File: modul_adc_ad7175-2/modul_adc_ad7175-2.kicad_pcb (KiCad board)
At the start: 2 copper layers, 61 x 55.9 mm, 9 parts

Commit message: Приступил к разводке платы c AD7175-2.
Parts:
- added C1: 4.7 мк, IWsmd_case:SMD0805, F.Cu at (76.5, 138.4)
- added C10: 270 п, IWsmd_case:SMD0805, F.Cu at (98.6, 114.3)
- added C11: 270 п, IWsmd_case:SMD0805, F.Cu at (95.5, 126.2)
- added C12: 270 п, IWsmd_case:SMD0805, F.Cu at (94.7, 133.1)
- added C13: 1.3 н, IWsmd_case:SMD0805, F.Cu at (94.2, 112.3)
- added C14: 1.3 н, IWsmd_case:SMD0805, F.Cu at (95.5, 130.0)
- added C15: 0.1 мк, IWsmd_case:SMD0805, F.Cu at (91.2, 130.8)
- added C16: 0.1 мк, IWsmd_case:SMD0805, F.Cu at (95.5, 118.7)
- added C17: 0.1 мк, IWsmd_case:SMD0805, F.Cu at (90.2, 112.9)
- added C18: 0.1 мк, IWsmd_case:SMD0805, F.Cu at (90.2, 115.2)
- added C2: 0.1 мк, IWsmd_case:SMD0805, F.Cu at (78.7, 138.4)
- added C21: 0.1 мк, IWsmd_case:SMD0805, F.Cu at (83.6, 124.0)
- added C22: 1 мк, IWsmd_case:SMD0805, F.Cu at (85.9, 124.0)
- added C23: 0.1 мк, IWsmd_case:SMD0805, F.Cu at (82.3, 109.0)
- added C24: 0.1 мк, IWsmd_case:SMD0805, F.Cu at (79.0, 125.2)
- added C25: 0.1 мк, IWsmd_case:SMD0805, F.Cu at (79.8, 109.0)
- added C26: 10 мк, IWsmd_case:CASE_B, F.Cu at (75.9, 126.2)
- added C27: 10 мк, IWsmd_case:CASE_B, F.Cu at (76.5, 108.0)
- added C28: 0.1 мк, IWsmd_case:SMD0805, F.Cu at (85.1, 109.0)
- added C29: 1 мк, IWsmd_case:SMD0805, F.Cu at (87.1, 109.0)
- added C3: 0.1 мк, IWsmd_case:SMD0805, F.Cu at (101.3, 106.2)
- added C4: 0.1 мк, IWsmd_case:SMD0805, F.Cu at (101.3, 126.2)
- added C5: 10 мк, IWsmd_case:CASE_B, F.Cu at (100.6, 103.1)
- added C6: 10 мк, IWsmd_case:CASE_B, F.Cu at (100.6, 123.2)
- added C7: 0.1 мк, IWsmd_case:SMD0805, F.Cu at (85.1, 133.7)
- added C8: 4.7 мк, IWsmd_case:SMD0805, F.Cu at (85.9, 130.3)
- added C9: 270 п, IWsmd_case:SMD0805, F.Cu at (94.5, 109.2)
- added DA1: AD8475BRMZ, IWsmd_case:MSOP-10, F.Cu at (102.4, 110.5)
- added DA2: AD8475BRMZ, IWsmd_case:MSOP-10, F.Cu at (102.4, 130.6)
- added DA3: ADR444BRZ, IWsmd_case:SOIC8, F.Cu at (79.5, 133.6)
- added DD1: AD7175-2, IWsmd_case:TSOP24, F.Cu at (83.1, 116.8)
- added R1: 0, IWsmd_case:SMD0805, F.Cu at (112.5, 105.2)
- added R10: 0, IWsmd_case:SMD0805, F.Cu at (82.5, 103.5)
- added R11: 0, IWsmd_case:SMD0805, F.Cu at (92.7, 103.5)
- added R12: 0, IWsmd_case:SMD0805, F.Cu at (112.5, 109.2)
- added R13: 0, IWsmd_case:SMD0805, F.Cu at (112.5, 129.5)
- added R14: 5 к 0.1%, IWsmd_case:SMD0805, F.Cu at (107.4, 112.0)
- added R15: 5 к 0.1%, IWsmd_case:SMD0805, F.Cu at (107.4, 114.0)
- added R16: 5 к 0.1%, IWsmd_case:SMD0805, F.Cu at (107.4, 106.4)
- added R17: 5 к 0.1%, IWsmd_case:SMD0805, F.Cu at (107.4, 108.5)
- added R18: 5 к 0.1%, IWsmd_case:SMD0805, F.Cu at (107.4, 132.3)
- added R19: 5 к 0.1%, IWsmd_case:SMD0805, F.Cu at (107.4, 134.4)
- added R2: 0, IWsmd_case:SMD0805, F.Cu at (112.5, 127.5)
- added R20: 5 к 0.1%, IWsmd_case:SMD0805, F.Cu at (107.4, 126.7)
- added R21: 5 к 0.1%, IWsmd_case:SMD0805, F.Cu at (107.4, 128.8)
- added R22: 0, IWsmd_case:SMD0805, F.Cu at (85.6, 136.9)
- added R23: 0, IWsmd_case:SMD0805, F.Cu at (73.4, 135.1)
- added R24: 0, IWsmd_case:SMD0805, F.Cu at (83.2, 141.3)
- added R25: 0, IWsmd_case:SMD0805, F.Cu at (95.9, 137.8)
- added R26: 0, IWsmd_case:SMD0805, F.Cu at (91.4, 137.8)
- added R27: 0, IWsmd_case:SMD0805, F.Cu at (101.9, 140.2)
- added R28: 10, IWsmd_case:SMD0805, F.Cu at (98.6, 109.2)
- added R29: 10, IWsmd_case:SMD0805, F.Cu at (98.6, 111.8)
- added R3: 0, IWsmd_case:SMD0805, F.Cu at (112.5, 111.3)
- added R30: 10, IWsmd_case:SMD0805, F.Cu at (98.6, 129.3)
- added R31: 10, IWsmd_case:SMD0805, F.Cu at (98.6, 131.8)
- added R32: 10 к 0.1%, IWsmd_case:SMD0805, F.Cu at (85.9, 128.0)
- added R33: 10 к 0.1%, IWsmd_case:SMD0805, F.Cu at (88.9, 130.8)
- added R34: 10 к, IWsmd_case:SMD0805, F.Cu at (95.1, 103.5)
- added R35: 10 к, IWsmd_case:SMD0805, F.Cu at (90.4, 108.7)
- added R4: 0, IWsmd_case:SMD0805, F.Cu at (112.5, 107.2)
- added R5: 0, IWsmd_case:SMD0805, F.Cu at (112.5, 131.6)
- added R6: 0, IWsmd_case:SMD0805, F.Cu at (112.5, 125.5)
- added R7: 0, IWsmd_case:SMD0805, F.Cu at (90.2, 103.5)
- added R8: 0, IWsmd_case:SMD0805, F.Cu at (87.6, 103.5)
- added R9: 0, IWsmd_case:SMD0805, F.Cu at (85.1, 103.5)
- added XP5: WF-3, IWconnectors:WF-3, F.Cu at (72.4, 140.5)
- added XP6: SMA-JR, IWconnectors:SMA-R, F.Cu at (119.4, 109.2)
- added XP7: SMA-JR, IWconnectors:SMA-R, F.Cu at (119.4, 129.5)
- C19, C20: value 12 п -> 9.1 п; footprint SMD0805 -> IWsmd_case:SMD0805
- Z1: value 2.4576 МГц -> FA-20H 16 МГц; footprint Q_49U3HMS& -> IWsmd_case:EPSON_FA-20H
- moved C20 29.2 mm to (71.4, 112.5), turned to 180 degrees
- moved C19 20.8 mm to (71.4, 119.1)
- moved Z1 20.6 mm to (71.4, 115.8), turned to 0 degrees
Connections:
- C19 pad 1: N-0000046 -> Net-(C19-Pad1)
- C19 pad 2: /GND -> /DGND
- C20 pad 1: N-0000041 -> Net-(C20-Pad1)
- C20 pad 2: /GND -> /DGND
- XP1 pad 7: (no net) -> Net-(XP1-Pad7)
- XP1 pad 8: (no net) -> Net-(XP1-Pad8)
- XP2 pad 1: (no net) -> Net-(XP2-Pad1)
- XP2 pad 2: (no net) -> Net-(XP2-Pad2)
- XP2 pad 3: (no net) -> Net-(XP2-Pad3)
- XP2 pad 4: (no net) -> Net-(XP2-Pad4)
- XP2 pad 8: (no net) -> Net-(XP2-Pad8)
- XP3 pad 1: (no net) -> Net-(XP3-Pad1)
- XP3 pad 2: (no net) -> Net-(XP3-Pad2)
- XP3 pad 6: (no net) -> Net-(XP3-Pad6)
- XP4 pad 2: (no net) -> /A1
- XP4 pad 3: (no net) -> /A2
- XP4 pad 4: (no net) -> /A3
- XP4 pad 5: (no net) -> /A4
- XP4 pad 6: (no net) -> /A5
- Z1 pad 1: N-0000041 -> Net-(C19-Pad1)
- Z1 pad 2: N-0000046 -> Net-(C20-Pad1)
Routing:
- net /AVCC: track 0.00 -> 118.7 mm, vias 0 -> 5
- net /DVCC: track 0.00 -> 108.8 mm, vias 0 -> 5
- net /AGND: track 0.00 -> 100.3 mm, vias 0 -> 13
- net /DGND: track 0.00 -> 99.9 mm, vias 0 -> 2
- net /VOCM: track 0.00 -> 47.2 mm, vias 0 -> 6
- net /REF+: track 0.00 -> 31.3 mm, vias 0 -> 2
- net /~SYNC~/ERR: track 0.00 -> 23.5 mm, vias 0 -> 2
- net /~CS: track 0.00 -> 21.8 mm, vias 0 -> 2
- net Net-(R2-Pad1): track 0.00 -> 21.7 mm
- net Net-(R1-Pad1): track 0.00 -> 21.7 mm
- net Net-(C13-Pad1): track 0.00 -> 20.7 mm
- net /SCLK: track 0.00 -> 20.6 mm, vias 0 -> 2
- net /MISO: track 0.00 -> 19.2 mm, vias 0 -> 2
- net Net-(C10-Pad2): track 0.00 -> 19.2 mm
- net Net-(C1-Pad1): track 0.00 -> 18.9 mm
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- added copper zone on B.Cu, net /AGND
- removed copper zone on B.Cu, net /GND
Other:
- net class Default: clearance 0.254 -> 0.25; trace_width 0.254 -> 0.25; via_dia 1.19888 -> 1.2; via_drill 0.59944 -> 0.6
- rule trace_clearance: 0.254 -> 0.25
- rule trace_min: 0.254 -> 0.2

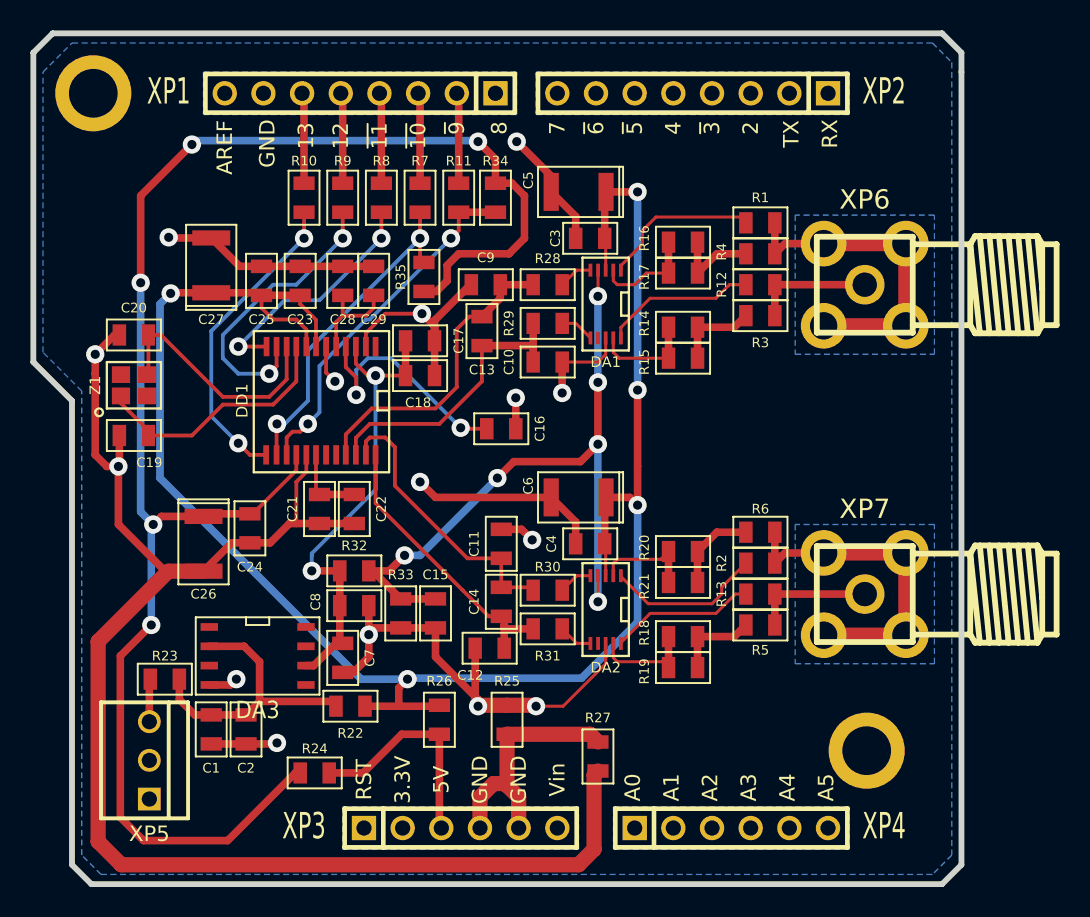
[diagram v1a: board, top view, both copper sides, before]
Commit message: Закончил разводку платы c AD7175-2.
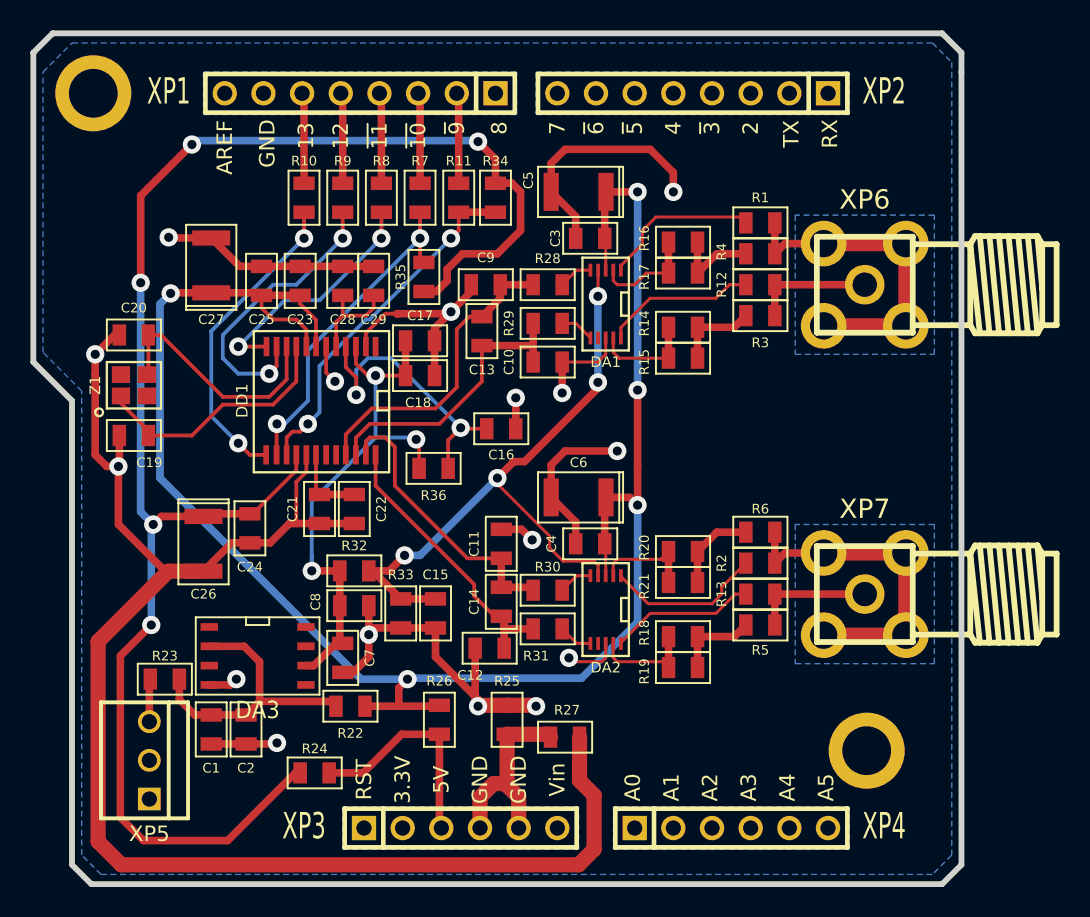
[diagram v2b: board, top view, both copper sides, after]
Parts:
- added R36: 0, IWsmd_case:SMD0805, F.Cu at (91.1, 121.3)
- moved R27 2.50 mm to (99.7, 138.9), turned to 180 degrees
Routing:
- net /REF+: track 31.3 -> 37.0 mm, vias 2 -> 3
- net /VOCM: track 47.2 -> 43.3 mm, vias 6 -> 4
- net /AGND: track 100.3 -> 103.7 mm, vias 13 -> 14
- net /GND: track 16.8 -> 13.6 mm
- net /REFOUT: track 15.9 -> 18.9 mm
- net /DGND: track 99.9 -> 102.4 mm
- net /DVCC: track 108.8 -> 108.0 mm
